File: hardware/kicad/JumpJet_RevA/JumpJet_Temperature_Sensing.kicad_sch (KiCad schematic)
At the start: 16 parts, among them J6 10k NTC OUT, J7 10k NTC CASE, J8 10k NTC CHAMBER, J9 10k NTC4 DNP

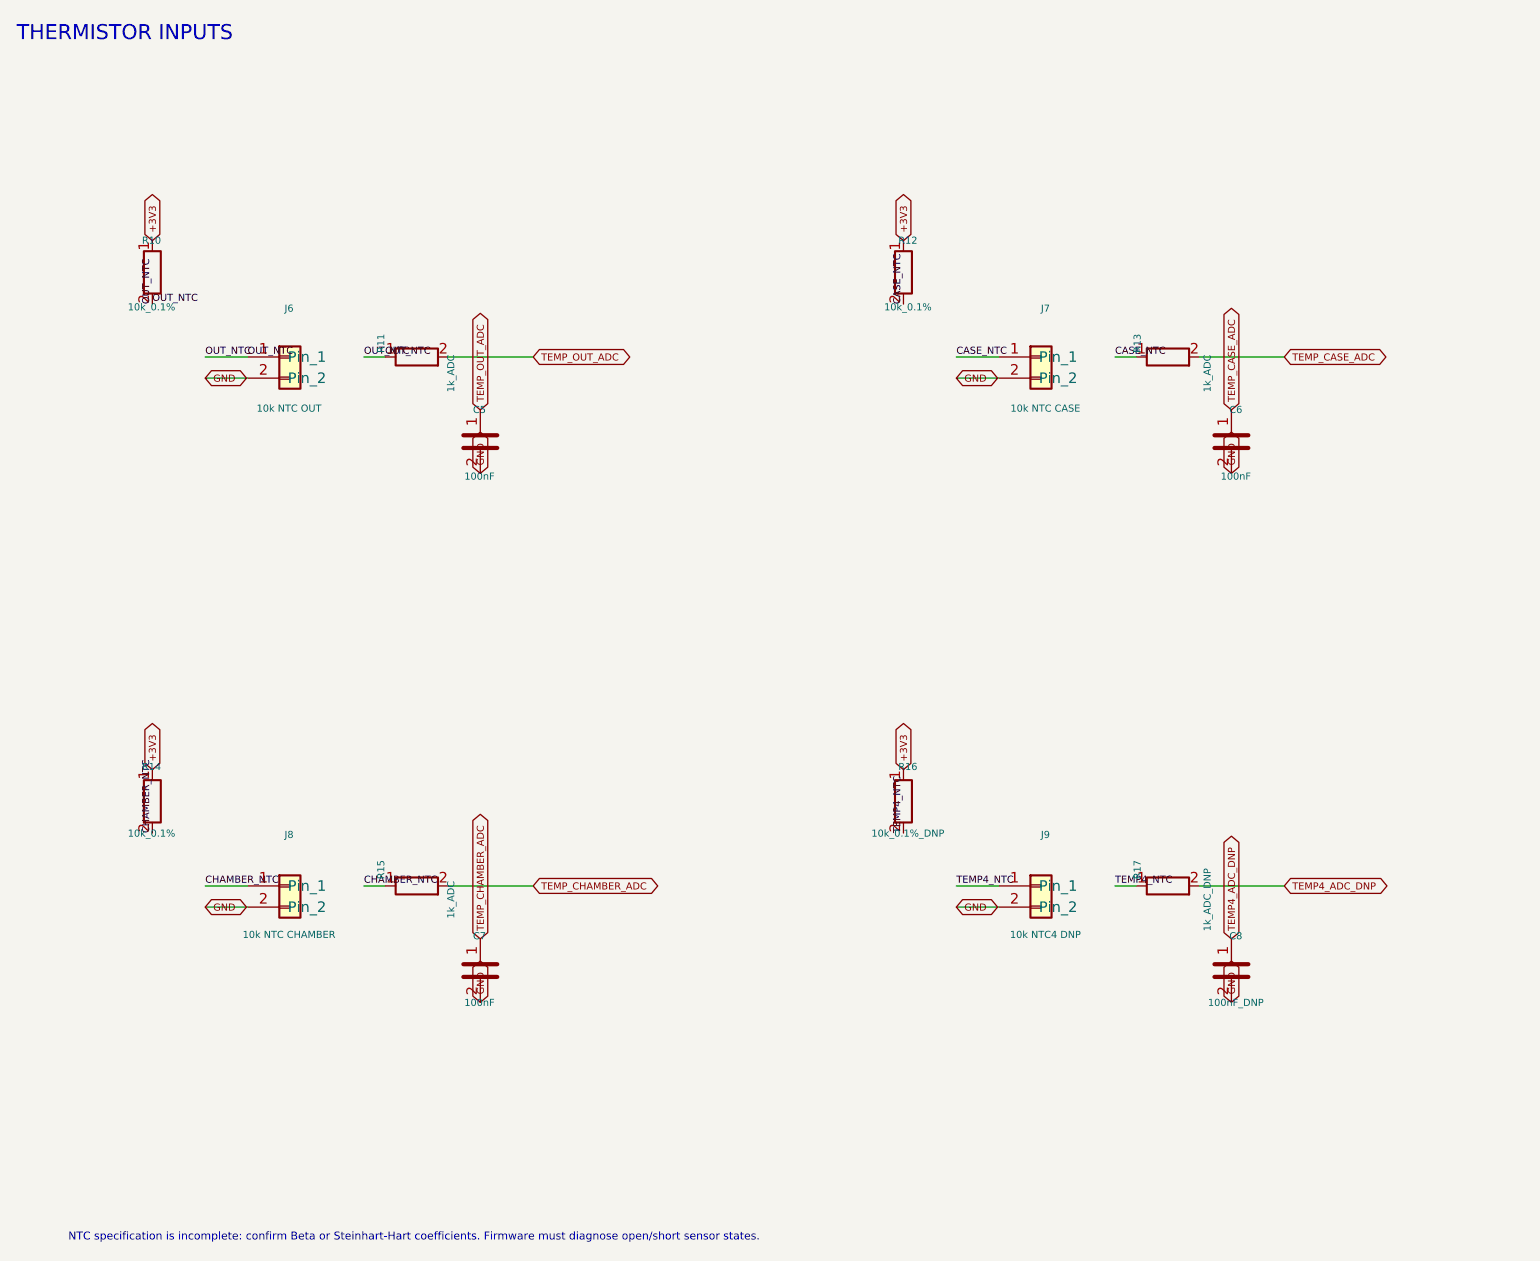
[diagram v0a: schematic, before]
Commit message: hardware: add onboard PCB thermistor channel
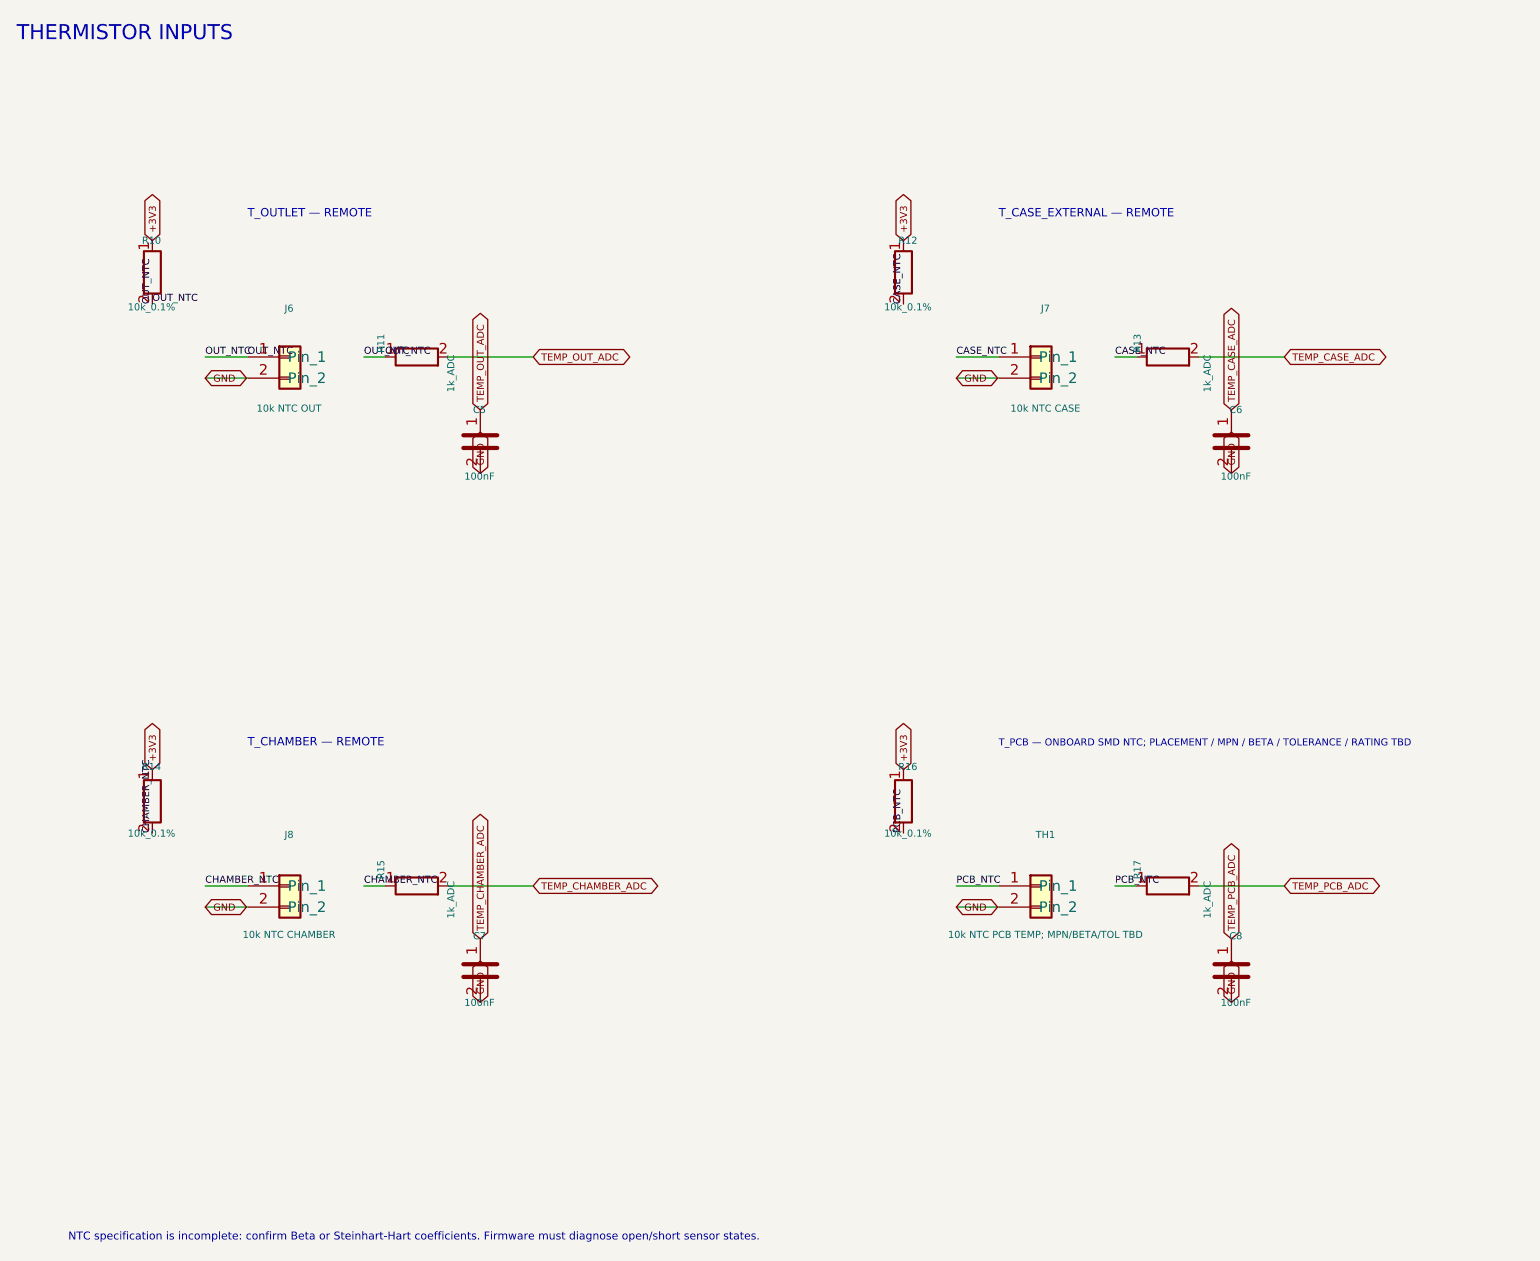
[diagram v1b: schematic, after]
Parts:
- C8: value 100nF_DNP -> 100nF
- R16: value 10k_0.1%_DNP -> 10k_0.1%
- R17: value 1k_ADC_DNP -> 1k_ADC
- TH1: renamed from J9; value 10k NTC4 DNP -> 10k NTC PCB TEMP; MPN/BETA/TOL TBD; footprint Connector_JST:JST_XH_B2B-XH-A_1x02_P2.50mm_Vertical -> Resistor_SMD:R_0603_1608Metric
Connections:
- net TEMP4_ADC_DNP renamed TEMP_PCB_ADC
- net TEMP4_NTC renamed PCB_NTC
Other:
- note added: "T_CASE_EXTERNAL — REMOTE"
- note added: "T_CHAMBER — REMOTE"
- note added: "T_OUTLET — REMOTE"
- note added: "T_PCB — ONBOARD SMD NTC; PLACEMENT / MPN / BETA / TOLERANCE / RATING TBD"
- title: JumpJet Controller — Thermistor front ends -> JumpJet Controller — Four-channel thermistor front ends
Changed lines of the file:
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@@
   (paper "A4" portrait)
   (title_block
-    (title "JumpJet Controller — Thermistor front ends")
+    (title "JumpJet Controller — Four-channel thermistor front ends")
     (date "2026-08-25")
     (rev "A.4.1 - LAYOUT CLEANUP")
@@
     (comment 1 "24 V PTC chamber-heater controller")
     (comment 2 "ESP32-S3 SuperMini 2x9 carrier; measured 23.7 x 17.93 mm, 25.0 mm incl. USB-C")
-    (comment 3 "TBD values require bench verification before assembly")
+    (comment 3 "Remote T_CHAMBER/T_OUTLET/T_CASE_EXTERNAL plus onboard T_PCB; ADC assignments TBD")
     (comment 4 "Heater thermal cutoffs are independent of firmware")
   )
@@
     (effects (font (size 0.95 0.95) (thickness 0.120)) (justify left bottom))
   )
-  (label "TEMP4_NTC" (at 153.67 123.19 0)
+  (text "T_OUTLET — REMOTE" (at 49.53 43.18 0)
+    (effects (font (size 1.0 1.0) (thickness 0.15)) (justify left bottom))
+  )
+  (text "T_CASE_EXTERNAL — REMOTE" (at 139.7 43.18 0)
+    (effects (font (size 1.0 1.0) (thickness 0.15)) (justify left bottom))
+  )
+  (text "T_CHAMBER — REMOTE" (at 49.53 106.68 0)
+    (effects (font (size 1.0 1.0) (thickness 0.15)) (justify left bottom))
+  )
+  (text "T_PCB — ONBOARD SMD NTC; PLACEMENT / MPN / BETA / TOLERANCE / RATING TBD" (at 139.7 106.68 0)
+    (effects (font (size 0.85 0.85) (thickness 0.12)) (justify left bottom))
+  )
+  (label "PCB_NTC" (at 153.67 123.19 0)
     (effects (font (size 0.85 0.85)) (justify left bottom))
   )
@@
     (effects (font (size 0.85 0.85)) (justify left bottom))
   )
-  (label "TEMP4_NTC" (at 128.27 116.84 90)
+  (label "PCB_NTC" (at 128.27 116.84 90)
     (effects (font (size 0.85 0.85)) (justify left bottom))
   )
@@
     (effects (font (size 0.85 0.85)) (justify left bottom))
   )
-  (label "TEMP4_NTC" (at 134.62 123.19 0)
+  (label "PCB_NTC" (at 134.62 123.19 0)
     (effects (font (size 0.85 0.85)) (justify left bottom))
   )
@@
     (effects (font (size 0.85 0.85)) (justify left bottom))
   )
-  (global_label "TEMP4_ADC_DNP" (shape bidirectional) (at 173.99 123.19 0) (fields_autoplaced)
+  (global_label "TEMP_PCB_ADC" (shape bidirectional) (at 173.99 123.19 0) (fields_autoplaced)
     (effects (font (size 0.85 0.85)) (justify left bottom))
   )
@@
     (effects (font (size 0.85 0.85)) (justify left bottom))
   )
-  (global_label "TEMP4_ADC_DNP" (shape bidirectional) (at 167.64 129.54 90) (fields_autoplaced)
+  (global_label "TEMP_PCB_ADC" (shape bidirectional) (at 167.64 129.54 90) (fields_autoplaced)
     (effects (font (size 0.85 0.85)) (justify left bottom))
   )
@@
   (symbol (lib_id "Connector_Generic:Conn_01x02") (at 144.78 123.19 0) (unit 1)
     (in_bom yes) (on_board yes) (dnp no)
-    (property "Reference" "J9" (at 145.31 117.04 0)
-      (effects (font (size 0.85 0.85)))
-    )
-    (property "Value" "10k NTC4 DNP" (at 145.31 129.04 0)
-      (effects (font (size 0.85 0.85)))
-    )
-    (property "Footprint" "Connector_JST:JST_XH_B2B-XH-A_1x02_P2.50mm_Vertical" (at 145.31 123.04 0)
+    (property "Reference" "TH1" (at 145.31 117.04 0)
+      (effects (font (size 0.85 0.85)))
+    )
+    (property "Value" "10k NTC PCB TEMP; MPN/BETA/TOL TBD" (at 145.31 129.04 0)
+      (effects (font (size 0.85 0.85)))
+    )
+    (property "Footprint" "Resistor_SMD:R_0603_1608Metric" (at 145.31 123.04 0)
       (effects (font (size 0.85 0.85)) hide)
     )
@@
       (effects (font (size 0.85 0.85)) hide)
     )
-    (property "Description" "" (at 145.31 123.04 0)
-      (effects (font (size 0.85 0.85)) hide)
-    )
-    (pin "1")
-    (pin "2")
-    (instances
-      (project "JumpJet_Controller_RevA4"
-        (path "/7c4d4b33-dd60-4c75-b093-7eaa23607d3f"
-          (reference "J9") (unit 1)
+    (property "Description" "Onboard PCB temperature NTC; exact production device and placement TBD" (at 145.31 123.04 0)
+      (effects (font (size 0.85 0.85)) hide)
+    )
+    (pin "1")
+    (pin "2")
+    (instances
+      (project "JumpJet_Controller_RevA4"
+        (path "/7c4d4b33-dd60-4c75-b093-7eaa23607d3f"
+          (reference "TH1") (unit 1)
         )
       )
@@
       (effects (font (size 0.85 0.85)))
     )
-    (property "Value" "10k_0.1%_DNP" (at 128.80 116.88 0)
+    (property "Value" "10k_0.1%" (at 128.80 116.88 0)
       (effects (font (size 0.85 0.85)))
     )
@@
       (effects (font (size 0.85 0.85)))
     )
-    (property "Value" "1k_ADC_DNP" (at 164.75 124.84 0)
+    (property "Value" "1k_ADC" (at 164.75 124.84 0)
       (effects (font (size 0.85 0.85)))
     )
@@
       (effects (font (size 0.85 0.85)))
     )
-    (property "Value" "100nF_DNP" (at 168.17 137.20 0)
-      (effects (font (size 0.85 0.85)))
-    )
+    (property "Value" "100nF" (at 168.17 137.20 0)
+      (effects (font (size 0.85 0.85)))
+    )
